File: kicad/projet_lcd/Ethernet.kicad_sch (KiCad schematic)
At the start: 49 parts, among them U1 LAN8742A-CZ-TR, U3 KMS-1102NL, Y1 25MHz

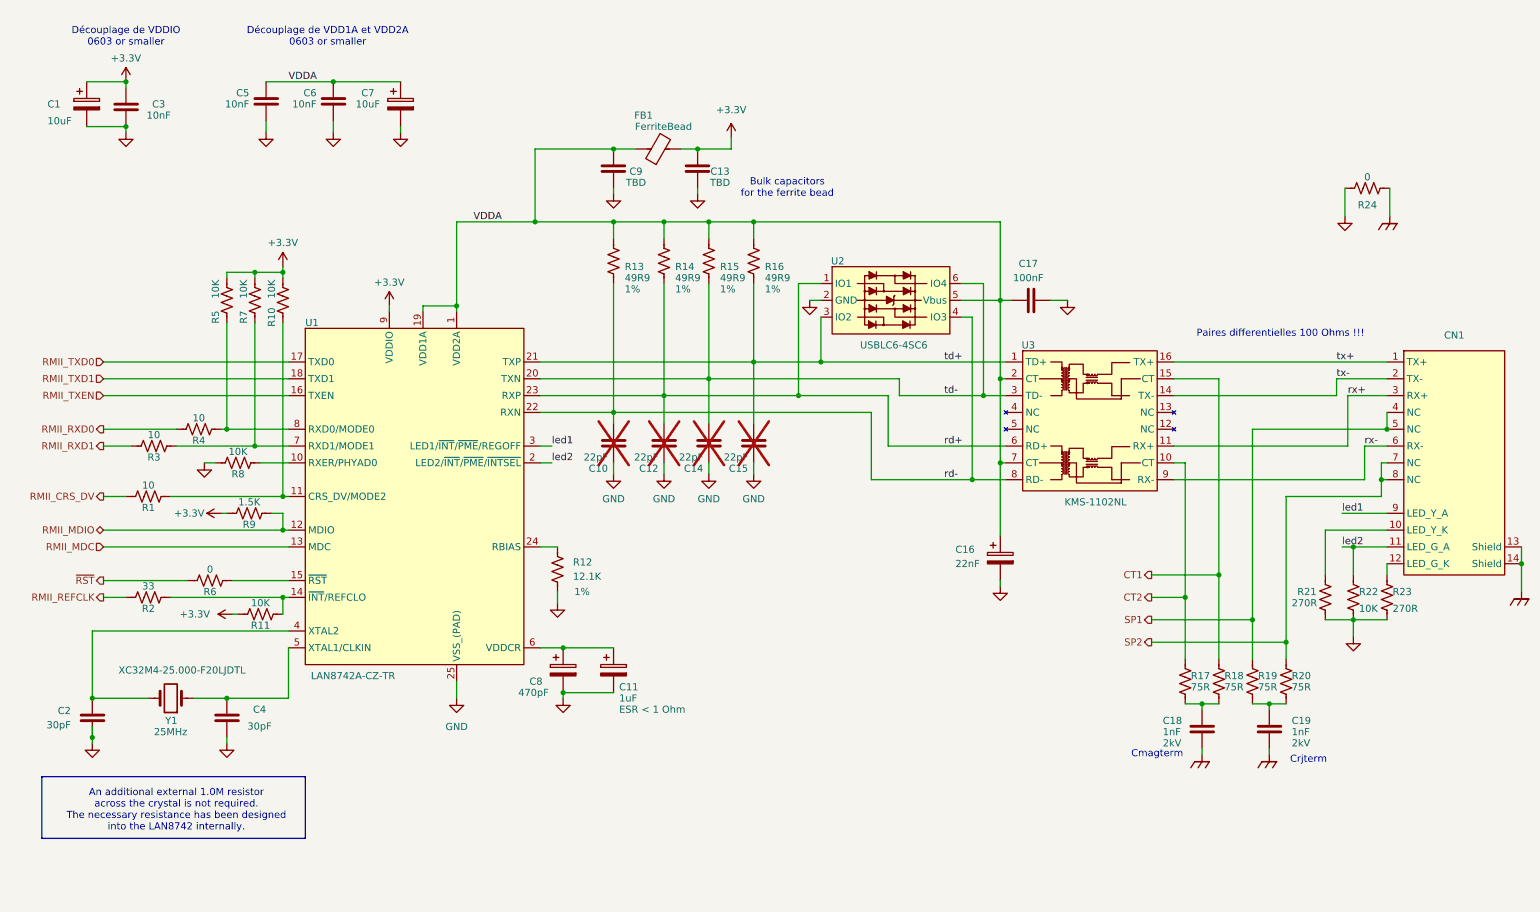
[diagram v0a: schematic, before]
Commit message: Removed all calls to old libs \o/
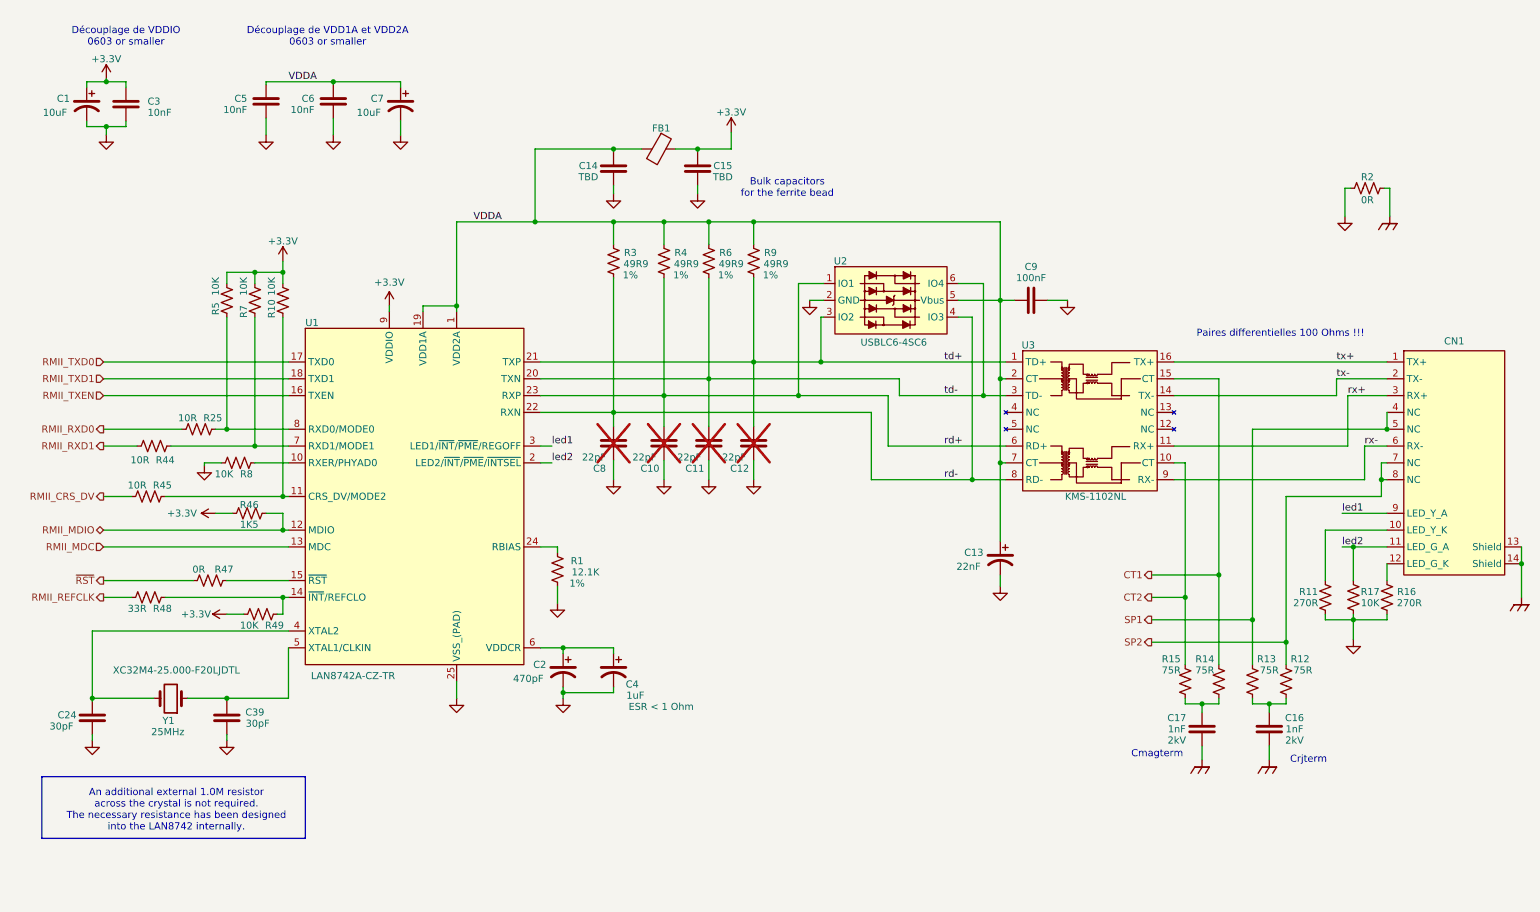
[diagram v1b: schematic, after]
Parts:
- removed C10, C12, C14, C15: 22pF, symbol Generiques:C
- removed C11: 1uF, symbol Generiques:C_Polarized
- removed C13, C9: TBD, symbol Generiques:C
- removed C16: 22nF, symbol Generiques:C_Polarized
- removed C17: 100nF, symbol Generiques:C
- removed C18, C19: 1nF, symbol Generiques:C
- removed C2, C4: 30pF, symbol Generiques:C
- removed C3, C5, C6: 10nF, symbol Generiques:C
- removed C7: 10uF, symbol Generiques:C_Polarized
- removed C8: 470pF, symbol Generiques:C_Polarized
- removed FB1: FerriteBead, symbol Generiques:FerriteBead
- removed R1, R3, R4: 10, symbol Generiques:R
- removed R10, R11, R22, R5, R7, R8: 10K, symbol Generiques:R
- removed R12: 12.1K, symbol Generiques:R
- removed R13, R14, R15, R16: 49R9, symbol Generiques:R
- removed R17, R18, R19, R20: 75R, symbol Generiques:R
- removed R2: 33, symbol Generiques:R
- removed R21, R23: 270R, symbol Generiques:R
- removed R24, R6: 0, symbol Generiques:R
- removed R9: 1.5K, symbol Generiques:R
- added C10, C11, C12, C8: 22pF, symbol Generics:C
- added C13: 22nF, symbol Generics:C_Polarized
- added C14, C15: TBD, symbol Generics:C
- added C16, C17: 1nF, symbol Generics:C
- added C2: 470pF, symbol Generics:C_Polarized
- added C24, C39: 30pF, symbol Generics:C
- added C3, C5, C6: 10nF, symbol Generics:C
- added C4: 1uF, symbol Generics:C_Polarized
- added C7: 10uF, symbol Generics:C_Polarized
- added C9: 100nF, symbol Generics:C
- added FB1: NI, symbol Generics:FB
- added R1: 12.1K, symbol Generics:R
- added R10, R17, R49, R5, R7, R8: 10K, symbol Generics:R
- added R11, R16: 270R, symbol Generics:R
- added R12, R13, R14, R15: 75R, symbol Generics:R
- added R2, R47: 0R, symbol Generics:R
- added R25, R44, R45: 10R, symbol Generics:R
- added R3, R4, R6, R9: 49R9, symbol Generics:R
- added R46: 1K5, symbol Generics:R
- added R48: 33R, symbol Generics:R
- C1: symbol Generiques:C_Polarized -> Generics:C_Polarized
- CN1: symbol Connectors:RJ45_with_Leds -> Generics:J_RJ45_w_Leds
- U2: symbol Diodes:USBLC6-4 -> Diodes:USBLC6-4SC6; Part# (none) -> USBLC6-4SC6; Ref USBLC6-4SC6 -> (none)
- U3: value KMS-1102NL -> ~; symbol Divers:KMS-1102NL -> Ethernet:KMS-1102NL; Part# (none) -> KMS-1102NL
- Y1: symbol Generiques:Crystal -> Generics:Y
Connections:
- net +3.3V: now also C1.P, C15.2, C3.2, FB1.1, R10.2 (1), R46.2 (1), R49.2 (1), R5.2 (1), R7.2 (1); no longer C1.1
- net CHASSIS: now also R2.2 (1); no longer CN1.13 (Shield), CN1.14 (Shield)
- net CT1: now also R14.2 (1)
- net CT2: now also R15.2 (1)
- net GND: now also C1.N, C10.2, C11.2, C12.2, C13.N, C14.1, C15.1, C2.N, C24.1, C3.1, C39.1, C4.N, C5.1, C6.1, C7.N, C8.2, C9.1, R1.1, R11.1, R16.1, R17.1, R2.1, R8.2 (1); no longer C1.2
- net RMII_CRS_DV: now also R45.2 (1)
- net RMII_MDIO: now also R46.1
- net RMII_REFCLK: now also R48.2 (1)
- net RMII_RXD0: now also R25.2 (1)
- net RMII_RXD1: now also R44.2 (1)
- net SP1: now also R13.2 (1)
- net SP2: now also R12.2 (1)
- net VDDA: now also C13.P, C14.2, C5.2, C6.2, C7.P, C9.2, FB1.2, R3.2 (1), R4.2 (1), R6.2 (1), R9.2 (1)
- net led2: now also R17.2 (1)
- net rd+: now also C10.1, R4.1
- net rd-: now also C8.1, R3.1
- net td+: now also C12.1, R9.1
- net td-: now also C11.1, R6.1
- net ~{RST}: now also R47.2 (1)
- net at U1.11 (CRS_DV/MODE2): now also R10.1, R45.1
- net at U1.15 (~{RST}): now also R47.1
- net at U1.5 (XTAL1/CLKIN), Y1.1: now also C39.2
- net at U1.24 (RBIAS): now also R1.2 (1)
- net at CN1.10 (LED_Y_K): now also R11.2 (1)
- net at U1.6 (VDDCR): now also C2.P, C4.P
- net at U1.8 (RXD0/MODE0): now also R25.1, R5.1
- net at U1.14 (~{INT}/REFCLO): now also R48.1, R49.1
- net at U1.10 (RXER/PHYAD0): now also R8.1
- net at U1.4 (XTAL2), Y1.2: now also C24.2
- net at U1.7 (RXD1/MODE1): now also R44.1, R7.1
- net at CN1.12 (LED_G_K): now also R16.2 (1)
- new net: C17.2, R14.1, R15.1
- new net: C16.2, R12.1, R13.1
- new net GND_CHASSIS: C16.1, C17.1, CN1.13 (Shield), CN1.14 (Shield)

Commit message: EOD
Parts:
- removed C5, C6: 10nF, symbol Generics:C
- removed C7: 10uF, symbol Generics:C_Polarized
- removed C9: 100nF, symbol Generics:C
- removed R10, R49, R7, R8: 10K, symbol Generics:R
- removed R4, R6, R9: 49R9, symbol Generics:R
- removed R44, R45: 10R, symbol Generics:R
- removed U1: LAN8742A-CZ-TR, symbol Chips:LAN8742A
- added C40: 100nF, Generics:C_0603, symbol Generics:C
- added C44: 10uF, Generics:C_0603, symbol Generics:C
- added C59, C60: 10nF, Generics:C_0603, symbol Generics:C
- added R21, R22, R23: 49R9, Generics:R_0402, symbol Generics:R
- added R25, R26, R29, R35: 10K, Generics:R_0402, symbol Generics:R
- added R28, R30: 10R, Generics:R_0402, symbol Generics:R
- added U8: ~, symbol Ethernet:LAN8742A
- C42: renamed from C1; footprint (none) -> Generics:C_0603; symbol Generics:C_Polarized -> Generics:C; LCSC Part # (none) -> C19702
- C43: renamed from C3; footprint (none) -> Generics:C_0603; LCSC Part # (none) -> C57112
- C45: renamed from C14; footprint (none) -> Generics:C_0603
- C46: renamed from C15; footprint (none) -> Generics:C_0603
- C48: renamed from C8; footprint (none) -> Generics:C_0603; LCSC Part # (none) -> C1653
- C49: renamed from C10; footprint (none) -> Generics:C_0603; LCSC Part # (none) -> C1653
- C50: renamed from C11; footprint (none) -> Generics:C_0603; LCSC Part # (none) -> C1653
- C51: renamed from C12; footprint (none) -> Generics:C_0603; LCSC Part # (none) -> C1653
- C54: renamed from C4; Comments ESR < 1 Ohm -> (none)
- C57: renamed from C17; Voltage 2kV -> (none)
- C58: renamed from C16; Voltage 2kV -> (none)
- R20: renamed from R3; footprint (none) -> Generics:R_0402; Comments 1% -> (none); LCSC Part # (none) -> C25120
- R24: renamed from R5; footprint (none) -> Generics:R_0402; LCSC Part # (none) -> C25744
- R27: renamed from R25; footprint (none) -> Generics:R_0402; LCSC Part # (none) -> C25077
- R33: renamed from R1; Comments 1% -> (none)
- Y3: renamed from Y1; Cl 20pF -> (none); REF XC32M4-25.000-F20LJDTL -> (none)
- renumbered C13 to C52, C2 to C53, C24 to C55, C39 to C56, FB1 to FB3, R2 to R19, R46 to R31, R47 to R32, R48 to R34, R11 to R36, R17 to R37, R16 to R38, R15 to R39, R14 to R40, R13 to R41, R12 to R42, U2 to U5, U3 to U7
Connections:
- net CHASSIS is gone; now on net GND_CHASSIS: R19.2 (1)
- net +3.3V: now also C42.2, R25.2 (1), R26.2 (1), R35.2 (1), U8.9 (VDDIO); no longer C42.P
- net GND: now also C42.1, C40.1, C44.1, C59.1, C60.1, R29.2 (1), U8.25 (VSS_(PAD)); no longer C42.N
- net RMII_CRS_DV: now also R30.2 (1)
- net RMII_MDC: now also U8.13 (MDC)
- net RMII_MDIO: now also U8.12 (MDIO)
- net RMII_RXD1: now also R28.2 (1)
- net RMII_TXD0: now also U8.17 (TXD0)
- net RMII_TXD1: now also U8.18 (TXD1)
- net RMII_TXEN: now also U8.16 (TXEN)
- net VDDA: now also C40.2, C44.2, C59.2, C60.2, R21.2 (1), R22.2 (1), R23.2 (1), U8.1 (VDD2A), U8.19 (VDD1A)
- net led1: now also U8.3 (LED1)
- net led2: now also U8.2 (LED2)
- net rd+: now also R21.1, U8.23 (RXP)
- net rd-: now also U8.22 (RXN)
- net td+: now also R23.1, U8.21 (TXP)
- net td-: now also R22.1, U8.20 (TXN)
- net at R34.1: now also R35.1, U8.14 (~{INT})
- net at C53.P, C54.P: now also U8.6 (VDDCR)
- net at C56.2, Y3.1: now also U8.5 (XTAL1)
- net at R24.1, R27.1: now also U8.8 (RXD0)
- net at C55.2, Y3.2: now also U8.4 (XTAL2)
- net at R32.1: now also U8.15 (~{RST})
- net at R33.2 (1): now also U8.24 (RBIAS)
- new net: R26.1, R30.1, U8.11 (CRS_DV)
- new net: R25.1, R28.1, U8.7 (RXD1)
- new net: R29.1, U8.10 (RXER)
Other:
- moved on the sheet: R36, R37, R38, R39, R40, R41, R42

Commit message: EOD
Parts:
- removed C40: 100nF, Generics:C_0603, symbol Generics:C
- removed C42, C44: 10uF, Generics:C_0603, symbol Generics:C
- removed C43: 10nF, Generics:C_0603, symbol Generics:C
- removed C45: TBD, Generics:C_0603, symbol Generics:C
- removed C49: 22pF, Generics:C_0603, symbol Generics:C
- removed C56: 30pF, symbol Generics:C
- removed CN1: ~, symbol Generics:J_RJ45_w_Leds
- removed R19: 0R, symbol Generics:R
- removed R22, R23: 49R9, Generics:R_0402, symbol Generics:R
- removed R40, R41: 75R, symbol Generics:R
- removed Y3: 25MHz, symbol Generics:Y
- added C52, C54: 100nF, Generics:C_0603, symbol Generics:C
- added C53: 1uF, Generics:C_0603, symbol Generics:C
- added C64, C65: 6pF, Generics:C_0402, symbol Generics:C
- added C67: 1nF, Generics:C_1206, symbol Generics:C
- added J2: ~, Connectors:R-RJ45R08P-C000, symbol Connectors:eth_R-RJ45R08P-C000
- added R26, R27, R28: 49R9, Generics:R_0402, symbol Generics:R
- added R43, R44: 75R, Generics:R_0603, symbol Generics:R
- added Y3: 25MHZ, Crystals:NX2016SA-25MHZ-STD-CZS-2, symbol Crystals:NX2016SA-25MHZ-STD-CZS-2
- C50: value 22pF -> 1uF; LCSC Part # C1653 -> C15849; now fitted
- C51: value 22pF -> 100nF; LCSC Part # C1653 -> C14663; now fitted
- C55: value 30pF -> 4.7uF; footprint (none) -> Generics:C_0603; LCSC Part # (none) -> C19666
- C56: renamed from C46; value TBD -> 4.7uF; LCSC Part # (none) -> C19666
- C57: renamed from C48; value 22pF -> 10pF; LCSC Part # C1653 -> (none)
- C58: value 1nF -> 10pF; footprint (none) -> Generics:C_0603; now not fitted
- C59, C60: value 10nF -> 10pF; LCSC Part # C57112 -> (none); now not fitted
- C61: renamed from C52; footprint (none) -> Generics:C_0402; symbol Generics:C_Polarized -> Generics:C; Comments (none) -> 50V; LCSC Part # (none) -> C1532
- C62: renamed from C53; footprint (none) -> Generics:C_0603; symbol Generics:C_Polarized -> Generics:C; LCSC Part # (none) -> C1620
- C63: renamed from C54; footprint (none) -> Generics:C_0603; symbol Generics:C_Polarized -> Generics:C; LCSC Part # (none) -> C15849
- C66: renamed from C57; footprint (none) -> Generics:C_1206; Comments (none) -> 2kV
- FB3: value NI -> ~; footprint (none) -> Generics:L_0805; Comments (none) -> 150mΩ ±25% 600Ω@100MHz 0805 Ferrite Beads ROHS; LCSC Part # (none) -> C2661857; Part# (none) -> 742792040
- R21: value 49R9 -> 0R; footprint Generics:R_0402 -> Generics:R_0805; LCSC Part # C25120 -> C17477
- R25: renamed from R20; Comments (none) -> 1.0%
- R33: renamed from R31; footprint (none) -> Generics:R_0402; LCSC Part # (none) -> C25867
- R34: renamed from R32; footprint (none) -> Generics:R_0402; LCSC Part # (none) -> C17168
- R35: renamed from R33; footprint (none) -> Generics:R_0603; LCSC Part # (none) -> C22864
- R36: renamed from R34; footprint (none) -> Generics:R_0402; LCSC Part # (none) -> C25105
- R37: footprint (none) -> Generics:R_0603; LCSC Part # (none) -> C25804
- R39: renamed from R36; footprint (none) -> Generics:R_0603; LCSC Part # (none) -> C22966
- R40: renamed from R38; footprint (none) -> Generics:R_0603; LCSC Part # (none) -> C22966
- R41: renamed from R39; footprint (none) -> Generics:R_0603; LCSC Part # (none) -> C4275
- R42: footprint (none) -> Generics:R_0603; LCSC Part # (none) -> C4275
- U5: footprint (none) -> Diodes:USBLC6-4; LCSC Part # (none) -> C111212
- U6: renamed from U8; footprint (none) -> Ethernet:LAN8742A-CZ-TR; LCSC Part # (none) -> C621424
- U7: footprint (none) -> Ethernet:KMS-1102NL; LCSC Part # (none) -> C19725172
- renumbered R24 to R22, R25 to R23, R26 to R24, R27 to R29, R28 to R30, R29 to R31, R30 to R32, R35 to R38
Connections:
- net +3.3V: now also FB3.2, C53.2, C54.2; no longer FB3.1
- net CT1: now also R42.2 (1)
- net GND: now also C50.1, C51.1, C58.2, C59.2, C60.2, C61.1, C62.1, C63.1, R21.1, C52.1, C53.1, C54.1, C64.1, C65.1, Y3.2 (GND), Y3.4 (GND); no longer C50.2, C51.2, C59.1, C60.1, C61.N, C62.N, C63.N
- net GND_CHASSIS: now also R21.2 (1), C67.1, J2.13 (Shield), J2.14 (Shield); no longer C58.1
- net SP1: now also J2.4 (NC), J2.5 (NC), R43.2 (1)
- net SP2: now also J2.7 (NC), J2.8 (NC), R44.2 (1); no longer R42.2 (1)
- net VDDA: now also C50.2, C51.2, C55.2, C61.2, FB3.1, C52.2, R26.2 (1), R27.2 (1), R28.2 (1); no longer C59.2, C60.2, C61.P, FB3.2, R21.2 (1)
- net led1: now also J2.9 (LED_Y_A)
- net led2: now also J2.11 (LED_G_A)
- net rx+: now also J2.3 (RX+)
- net rx-: now also J2.6 (RX-)
- net tx+: now also J2.1 (TX+)
- net tx-: now also J2.2 (TX-)
- net at C66.2, R41.1: now also R42.1
- net at U6.5 (XTAL1): now also C65.2, Y3.3
- net at U6.4 (XTAL2): now also C64.2, Y3.1; no longer C55.2
- net at R39.2 (1): now also J2.10 (LED_Y_K)
- net at R40.2 (1): now also J2.12 (LED_G_K)
- net rd+: no longer names the net of U5.1 (IO1), U6.23 (RXP), U7.6 (RD+)
- net rd+: now also C58.1, R26.1; no longer R21.1
- net rd-: no longer names the net of C57.1, R25.1, U5.4 (IO3), U6.22 (RXN), U7.8 (RD-)
- net td+: no longer names the net of U5.3 (IO2), U6.21 (TXP), U7.1 (TD+)
- net td+: now also C60.1, R28.1; no longer C51.1
- net td-: no longer names the net of U5.6 (IO4), U6.20 (TXN), U7.3 (TD-)
- net td-: now also C59.1, R27.1; no longer C50.1
- new net: C67.2, R43.1, R44.1
- new net: C62.2, C63.2, U6.6 (VDDCR)
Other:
- note added: "Ethernet"
- note removed: "Bulk capacitors for the ferrite bead"
- moved on the sheet: C56, C57, C66, R25, R37, R38, R39, R40, R41, U5

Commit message: EOD \o/
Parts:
- renumbered C50 to C57, C51 to C58, C52 to C59, C53 to C60, C54 to C61, C55 to C62, C56 to C63, C57 to C64, C58 to C65, C59 to C66, C60 to C67, C61 to C68, C62 to C69, C63 to C70, C64 to C71, C65 to C72, C66 to C73, C67 to C74, J2 to J3, R38 to R37, R39 to R38, R37 to R39
